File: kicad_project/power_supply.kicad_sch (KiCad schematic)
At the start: 1 part, among them J201 ATX-20

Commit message: playground start
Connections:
- net +3.3v renamed +3V3
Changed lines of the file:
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@@
 (kicad_sch (version 20211123) (generator eeschema)
   (paper "A4")
-  (wire (pts (xy 57.15 95.25) (xy 57.15 97.155))
+  (junction (at 76.2 72.39) (diameter 0) (color 0 0 0 0)
+  )
+  (junction (at 86.36 77.47) (diameter 0) (color 0 0 0 0)
+  )
+  (junction (at 76.2 58.42) (diameter 0) (color 0 0 0 0)
+  )
+  (junction (at 86.36 58.42) (diameter 0) (color 0 0 0 0)
+  )
+  (junction (at 102.87 58.42) (diameter 0) (color 0 0 0 0)
+  )
+  (junction (at 102.87 82.55) (diameter 0) (color 0 0 0 0)
+  )
+  (junction (at 57.15 95.885) (diameter 0) (color 0 0 0 0)
+  )
+  (wire (pts (xy 76.2 58.42) (xy 76.2 72.39))
     (stroke (width 0) (type default) (color 0 0 0 0))
   )
-  (wire (pts (xy 83.82 74.93) (xy 69.85 74.93))
+  (wire (pts (xy 57.15 95.25) (xy 57.15 95.885))
     (stroke (width 0) (type default) (color 0 0 0 0))
   )
-  (wire (pts (xy 69.85 82.55) (xy 89.535 82.55))
+  (wire (pts (xy 109.22 72.39) (xy 76.2 72.39))
     (stroke (width 0) (type default) (color 0 0 0 0))
   )
-  (wire (pts (xy 93.98 77.47) (xy 69.85 77.47))
+  (wire (pts (xy 76.2 74.93) (xy 69.85 74.93))
     (stroke (width 0) (type default) (color 0 0 0 0))
   )
-  (wire (pts (xy 83.82 57.15) (xy 83.82 74.93))
+  (wire (pts (xy 69.85 82.55) (xy 102.87 82.55))
     (stroke (width 0) (type default) (color 0 0 0 0))
   )
-  (wire (pts (xy 93.98 57.15) (xy 93.98 77.47))
+  (wire (pts (xy 109.22 77.47) (xy 86.36 77.47))
     (stroke (width 0) (type default) (color 0 0 0 0))
   )
-  (hierarchical_label "+3.3v" (shape output) (at 89.535 82.55 0)
+  (wire (pts (xy 57.15 95.885) (xy 57.15 97.155))
+    (stroke (width 0) (type default) (color 0 0 0 0))
+  )
+  (wire (pts (xy 86.36 77.47) (xy 69.85 77.47))
+    (stroke (width 0) (type default) (color 0 0 0 0))
+  )
+  (wire (pts (xy 102.87 57.15) (xy 102.87 58.42))
+    (stroke (width 0) (type default) (color 0 0 0 0))
+  )
+  (wire (pts (xy 109.22 95.885) (xy 57.15 95.885))
+    (stroke (width 0) (type default) (color 0 0 0 0))
+  )
+  (wire (pts (xy 102.87 82.55) (xy 109.22 82.55))
+    (stroke (width 0) (type default) (color 0 0 0 0))
+  )
+  (wire (pts (xy 76.2 57.15) (xy 76.2 58.42))
+    (stroke (width 0) (type default) (color 0 0 0 0))
+  )
+  (wire (pts (xy 86.36 57.15) (xy 86.36 58.42))
+    (stroke (width 0) (type default) (color 0 0 0 0))
+  )
+  (wire (pts (xy 76.2 72.39) (xy 76.2 74.93))
+    (stroke (width 0) (type default) (color 0 0 0 0))
+  )
+  (wire (pts (xy 102.87 58.42) (xy 102.87 82.55))
+    (stroke (width 0) (type default) (color 0 0 0 0))
+  )
+  (wire (pts (xy 86.36 58.42) (xy 86.36 77.47))
+    (stroke (width 0) (type default) (color 0 0 0 0))
+  )
+  (hierarchical_label "+5V" (shape output) (at 109.22 77.47 0)
     (effects (font (size 1.27 1.27)) (justify left))
   )
-  (symbol (lib_id "power:+5V") (at 93.98 57.15 0) (unit 1)
+  (hierarchical_label "GND" (shape output) (at 109.22 95.885 0)
+    (effects (font (size 1.27 1.27)) (justify left))
+  )
+  (hierarchical_label "+12V" (shape output) (at 109.22 72.39 0)
+    (effects (font (size 1.27 1.27)) (justify left))
+  )
+  (hierarchical_label "+3.3v" (shape output) (at 109.22 82.55 0)
+    (effects (font (size 1.27 1.27)) (justify left))
+  )
+  (symbol (lib_id "power:PWR_FLAG") (at 102.87 58.42 270) (mirror x) (unit 1)
     (in_bom yes) (on_board yes) (fields_autoplaced)
-    (property "Reference" "#PWR0114" (id 0) (at 93.98 60.96 0)
+    (property "Reference" "#FLG0203" (id 0) (at 104.775 58.42 0)
       (effects (font (size 1.27 1.27)) hide)
     )
-    (property "Value" "+5V" (id 1) (at 93.98 51.435 0))
-    (property "Footprint" "" (id 2) (at 93.98 57.15 0)
+    (property "Value" "PWR_FLAG" (id 1) (at 106.68 58.4199 90)
+      (effects (font (size 1.27 1.27)) (justify left))
+    )
+    (property "Footprint" "" (id 2) (at 102.87 58.42 0)
       (effects (font (size 1.27 1.27)) hide)
     )
-    (property "Datasheet" "" (id 3) (at 93.98 57.15 0)
+    (property "Datasheet" "~" (id 3) (at 102.87 58.42 0)
+      (effects (font (size 1.27 1.27)) hide)
+    )
+    (pin "1")
+  )
+  (symbol (lib_id "power:+5V") (at 86.36 57.15 0) (unit 1)
+    (in_bom yes) (on_board yes) (fields_autoplaced)
+    (property "Reference" "#PWR0114" (id 0) (at 86.36 60.96 0)
+      (effects (font (size 1.27 1.27)) hide)
+    )
+    (property "Value" "+5V" (id 1) (at 86.36 51.435 0))
+    (property "Footprint" "" (id 2) (at 86.36 57.15 0)
+      (effects (font (size 1.27 1.27)) hide)
+    )
+    (property "Datasheet" "" (id 3) (at 86.36 57.15 0)
+      (effects (font (size 1.27 1.27)) hide)
+    )
+    (pin "1")
+  )
+  (symbol (lib_id "power:PWR_FLAG") (at 86.36 58.42 270) (mirror x) (unit 1)
+    (in_bom yes) (on_board yes) (fields_autoplaced)
+    (property "Reference" "#FLG0202" (id 0) (at 88.265 58.42 0)
+      (effects (font (size 1.27 1.27)) hide)
+    )
+    (property "Value" "" (id 1) (at 90.17 58.4199 90)
+      (effects (font (size 1.27 1.27)) (justify left))
+    )
+    (property "Footprint" "" (id 2) (at 86.36 58.42 0)
+      (effects (font (size 1.27 1.27)) hide)
+    )
+    (property "Datasheet" "~" (id 3) (at 86.36 58.42 0)
+      (effects (font (size 1.27 1.27)) hide)
+    )
+    (pin "1")
+  )
+  (symbol (lib_id "power:+3V3") (at 102.87 57.15 0) (unit 1)
+    (in_bom yes) (on_board yes) (fields_autoplaced)
+    (property "Reference" "#PWR0202" (id 0) (at 102.87 60.96 0)
+      (effects (font (size 1.27 1.27)) hide)
+    )
+    (property "Value" "" (id 1) (at 102.87 52.07 0))
+    (property "Footprint" "" (id 2) (at 102.87 57.15 0)
+      (effects (font (size 1.27 1.27)) hide)
+    )
+    (property "Datasheet" "" (id 3) (at 102.87 57.15 0)
       (effects (font (size 1.27 1.27)) hide)
     )
@@
     (pin "1")
   )
-  (symbol (lib_id "power:+12V") (at 83.82 57.15 0) (unit 1)
+  (symbol (lib_id "power:+12V") (at 76.2 57.15 0) (unit 1)
     (in_bom yes) (on_board yes) (fields_autoplaced)
-    (property "Reference" "#PWR0113" (id 0) (at 83.82 60.96 0)
+    (property "Reference" "#PWR0113" (id 0) (at 76.2 60.96 0)
       (effects (font (size 1.27 1.27)) hide)
     )
-    (property "Value" "+12V" (id 1) (at 83.82 51.435 0))
-    (property "Footprint" "" (id 2) (at 83.82 57.15 0)
+    (property "Value" "+12V" (id 1) (at 76.2 51.435 0))
+    (property "Footprint" "" (id 2) (at 76.2 57.15 0)
       (effects (font (size 1.27 1.27)) hide)
     )
-    (property "Datasheet" "" (id 3) (at 83.82 57.15 0)
+    (property "Datasheet" "" (id 3) (at 76.2 57.15 0)
       (effects (font (size 1.27 1.27)) hide)
     )
+    (pin "1")
+  )
+  (symbol (lib_id "power:PWR_FLAG") (at 76.2 58.42 90) (unit 1)
+    (in_bom yes) (on_board yes) (fields_autoplaced)
+    (property "Reference" "#FLG0201" (id 0) (at 74.295 58.42 0)
+      (effects (font (size 1.27 1.27)) hide)
+    )
+    (property "Value" "" (id 1) (at 72.39 58.4199 90)
+      (effects (font (size 1.27 1.27)) (justify left))
+    )
+    (property "Footprint" "" (id 2) (at 76.2 58.42 0)
+      (effects (font (size 1.27 1.27)) hide)
+    )
+    (property "Datasheet" "~" (id 3) (at 76.2 58.42 0)
+      (effects (font (size 1.27 1.27)) hide)
+    )

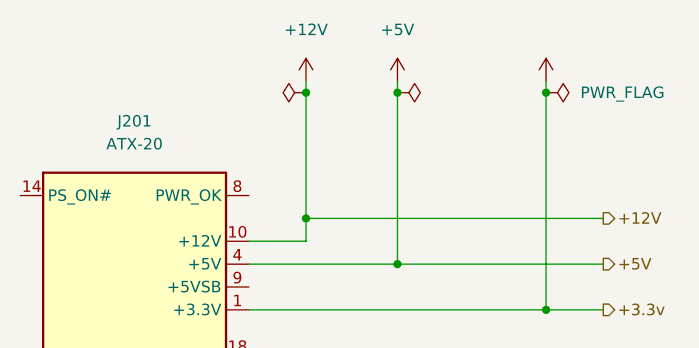
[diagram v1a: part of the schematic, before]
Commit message: added ecp5 fpga without anything connected yet, added power to fpga
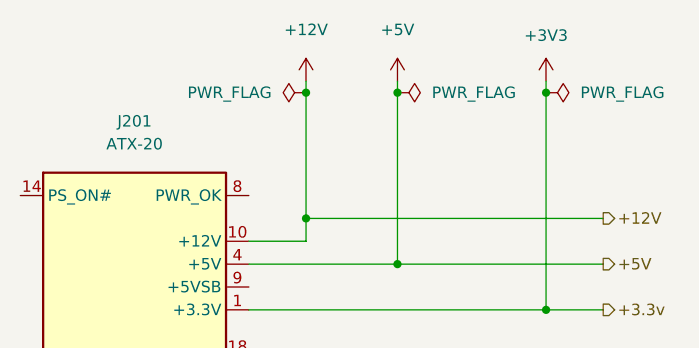
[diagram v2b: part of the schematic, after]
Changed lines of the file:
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@@
       (effects (font (size 1.27 1.27)) hide)
     )
-    (property "Value" "" (id 1) (at 90.17 58.4199 90)
+    (property "Value" "PWR_FLAG" (id 1) (at 90.17 58.4199 90)
       (effects (font (size 1.27 1.27)) (justify left))
     )
@@
       (effects (font (size 1.27 1.27)) hide)
     )
-    (property "Value" "" (id 1) (at 102.87 52.07 0))
+    (property "Value" "+3V3" (id 1) (at 102.87 52.07 0))
     (property "Footprint" "" (id 2) (at 102.87 57.15 0)
       (effects (font (size 1.27 1.27)) hide)
@@
       (effects (font (size 1.27 1.27)) hide)
     )
-    (property "Value" "" (id 1) (at 72.39 58.4199 90)
+    (property "Value" "PWR_FLAG" (id 1) (at 72.39 58.4199 90)
       (effects (font (size 1.27 1.27)) (justify left))
     )

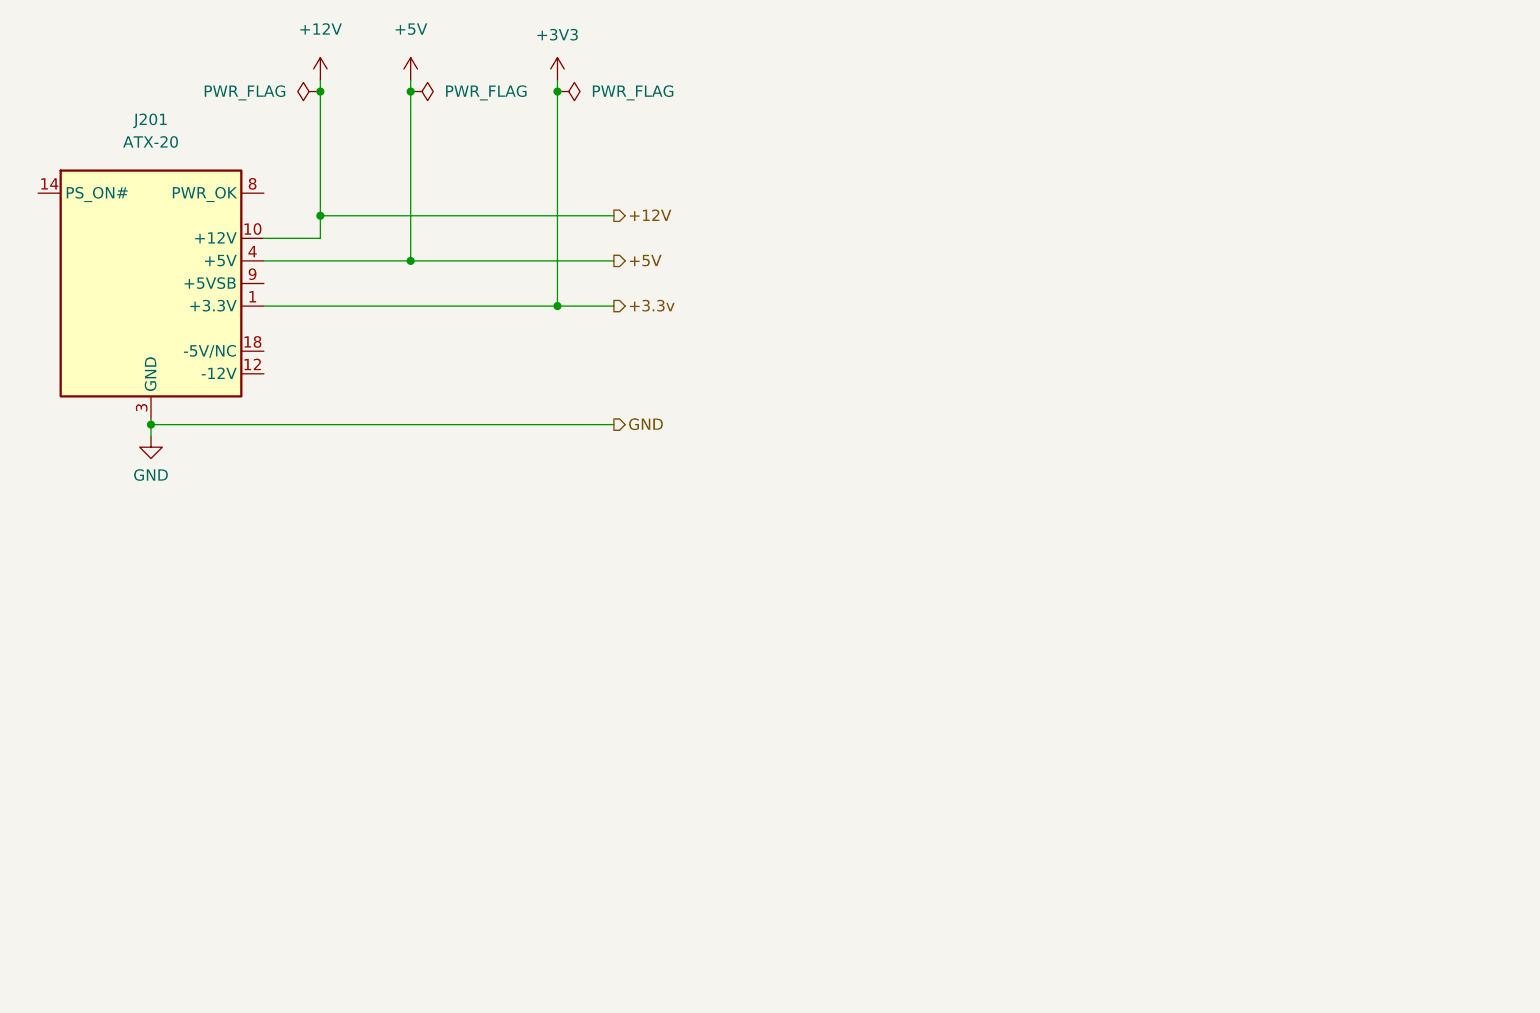
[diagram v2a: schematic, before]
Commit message: added bits and pieces: a bit of memory, a bit of 1.1V power
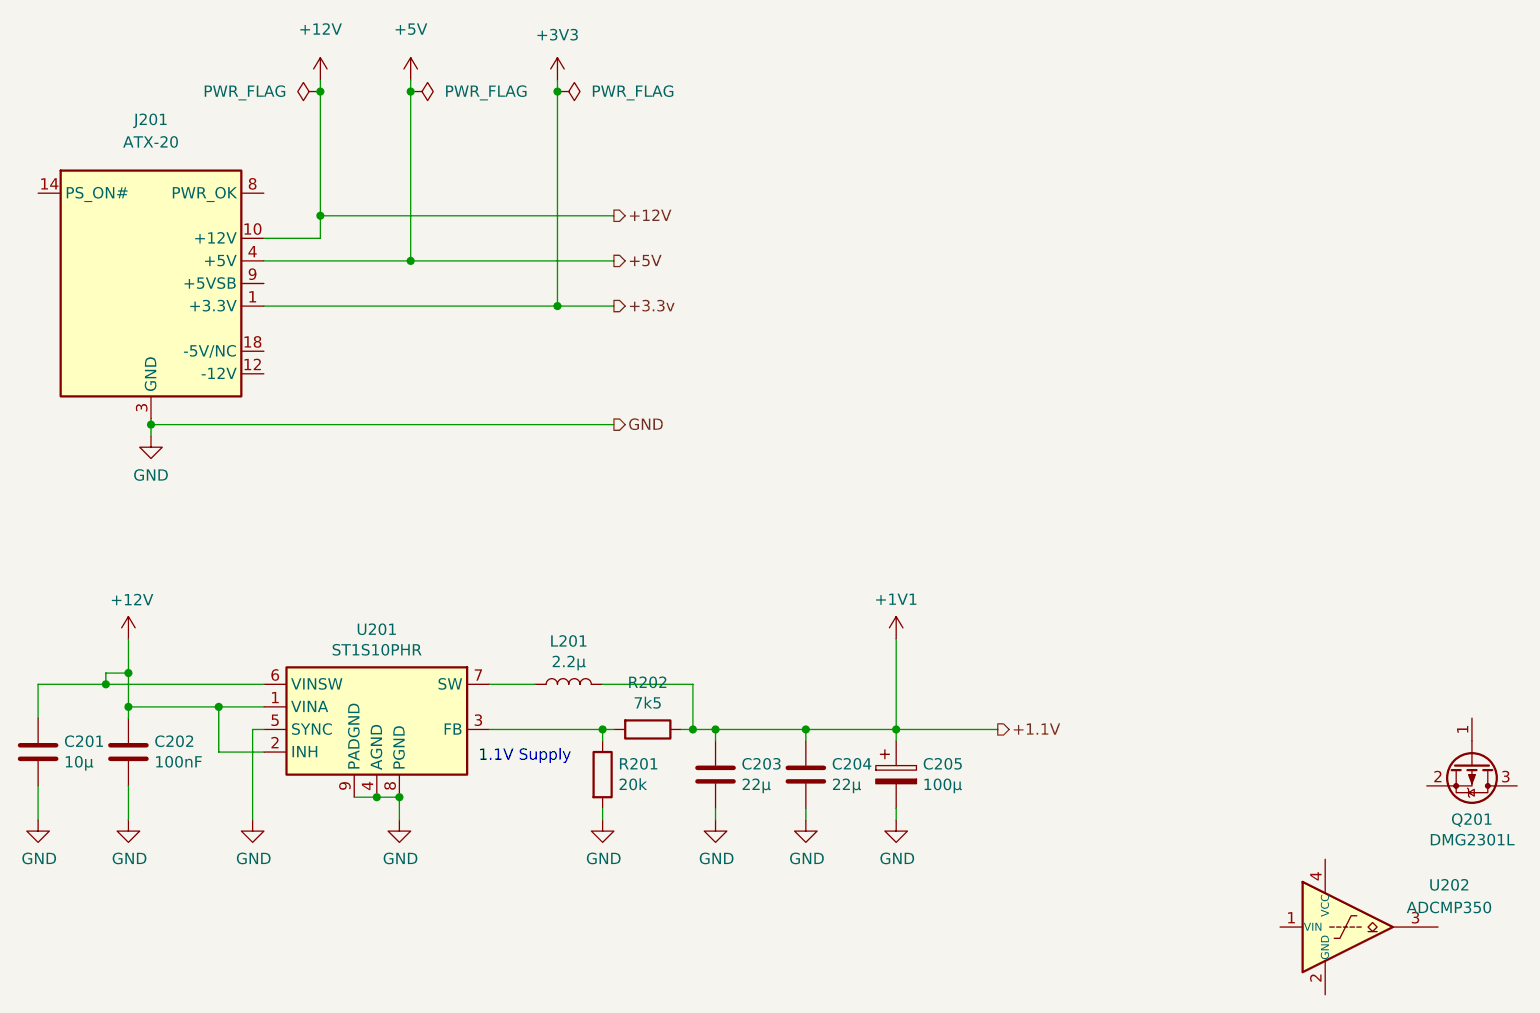
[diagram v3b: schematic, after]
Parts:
- added C201: 10µ, Capacitor_SMD:C_0603_1608Metric, symbol Device:C
- added C202: 100nF, Capacitor_SMD:C_0603_1608Metric, symbol Device:C
- added C203, C204: 22µ, Capacitor_SMD:C_0603_1608Metric, symbol Device:C
- added C205: 100µ, Capacitor_SMD:CP_Elec_5x5.9, symbol FPGA_PCIe-rescue:CP-Device
- added L201: 2.2µ, Inductor_SMD:L_Wuerth_MAPI-4030, symbol Device:L
- added Q201: DMG2301L, Package_TO_SOT_SMD:SOT-23, symbol Transistor_FET:DMG2301L
- added R201: 20k, Resistor_SMD:R_0603_1608Metric, symbol Device:R
- added R202: 7k5, Resistor_SMD:R_0603_1608Metric, symbol Device:R
- added U201: ST1S10PHR, Package_SO:TI_SO-PowerPAD-8, symbol Regulator_Switching:ST1S10PHR
- added U202: ADCMP350, Package_TO_SOT_SMD:Analog_KS-4, symbol Comparator:ADCMP350
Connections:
- net +12V: now also C201.1, C202.1, U201.1 (VINA), U201.2 (INH), U201.6 (VINSW)
- net GND: now also C201.2, C202.2, C203.2, C204.2, C205.2, R201.2, U201.4 (AGND), U201.5 (SYNC), U201.8 (PGND), U201.9 (PADGND)
- new net: R201.1, R202.2, U201.3 (FB)
- new net: L201.1, U201.7 (SW)
- new net +1V1: C203.1, C204.1, C205.1, L201.2, R202.1
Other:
- note added: "1.1V Supply"
